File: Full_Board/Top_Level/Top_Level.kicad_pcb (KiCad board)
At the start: 2 copper layers, 174 x 97.8 mm, 223 parts, among them IC1 DRV8824QPWPRQ1, IC2 DRV8824QPWPRQ1, IC3 DRV8824QPWPRQ1, IC5 CD74HC4051PWT, IC6 CD74HC4051PWT, J1 OQ0212500000G, J1-J3 Conn_01x10, J10 KLDHCX-8-0202-A, J11 OQ0212500000G, J12 OQ0432500000G, J13 OQ0432500000G, J14 OQ0432500000G, J16 OQ0432500000G, J17 OQ0432500000G, J18 OQ0432500000G, J19 OQ0432500000G, J2 OQ0212500000G, J20 OQ0212500000G, J21 OQ0212500000G, J22 OQ0212500000G, J23 OQ0212500000G, J4-J2 Conn_01x10, J5-J7 Conn_01x10, J7 OQ0212500000G, J8 OQ0212500000G, J8-J6 Conn_01x10, J9 OQ0212500000G, U1 UCLAMP3301H.TCT, U10 LM2576SX-3.3-NOPB, U11 UCLAMP3301H.TCT, U12 UCLAMP3301H.TCT, U13 UCLAMP3301H.TCT, U14 UCLAMP3301H.TCT, U15 UCLAMP3301H.TCT, U16 UCLAMP3301H.TCT, U17 UCLAMP3301H.TCT, U18 UCLAMP3301H.TCT, U2 UCLAMP3301H.TCT, U3 UCLAMP3301H.TCT, U4 UCLAMP3301H.TCT, U5 UCLAMP3301H.TCT, U6 UCLAMP3301H.TCT, U7 JS102011SCQN, U8 UCLAMP3301H.TCT, U9 UCLAMP3301H.TCT

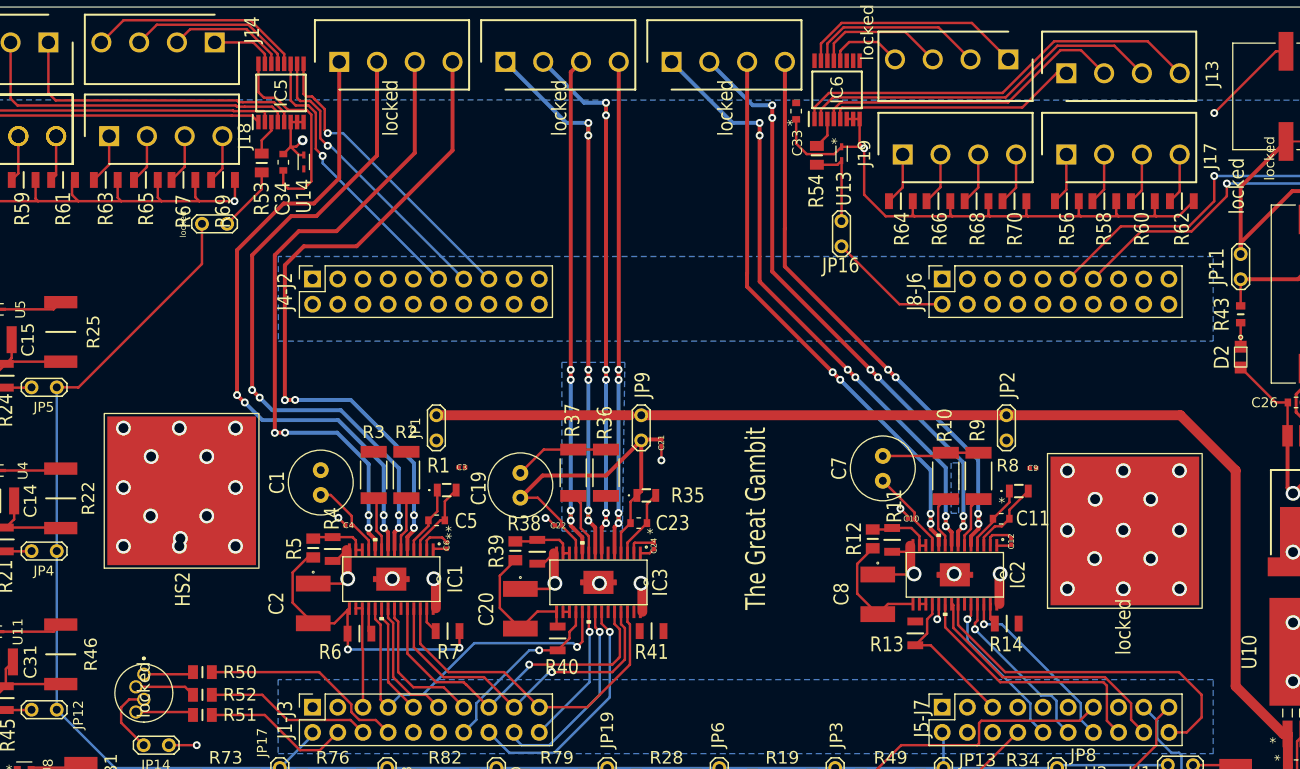
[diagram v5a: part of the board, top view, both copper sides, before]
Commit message: Only the truly awful traces left
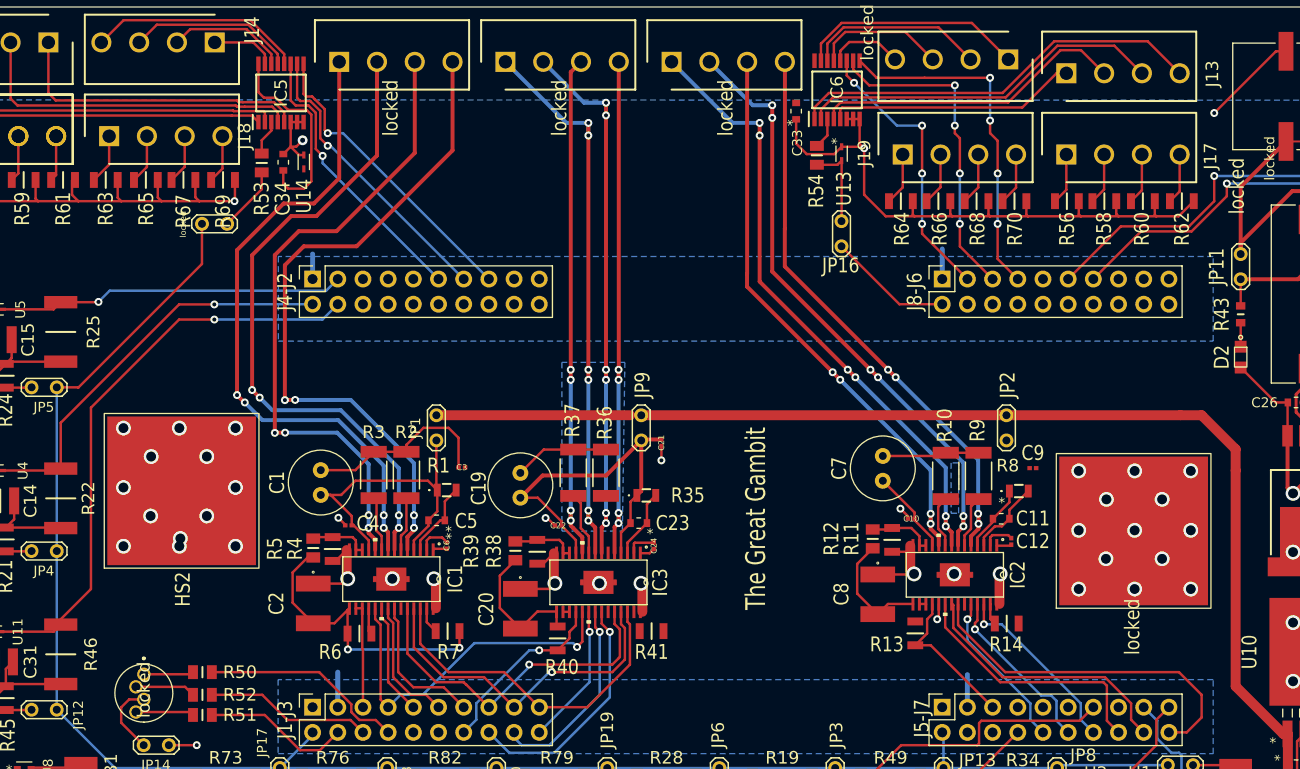
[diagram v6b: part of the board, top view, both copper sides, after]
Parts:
- moved locked 0.89 mm to (178.8, 91.4)
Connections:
- HS2 pad 1: (no net) -> GND
- J4-J2 pad 6: Y_HOME -> Y_FAULT
- J4-J2 pad 8: Y_FAULT -> Y_HOME
- locked pad 1: (no net) -> GND
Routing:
- net START_OUT: track 6.33 -> 58.7 mm, vias 0 -> 1
- net MUX_S2: track 0.00 -> 35.3 mm, vias 0 -> 4
- net RESET_OUT: track 5.95 -> 40.9 mm, vias 0 -> 1
- net MUX_S1: track 0.00 -> 32.9 mm, vias 0 -> 4
- net GND: track 428.4 -> 460.3 mm
- net HOME_OUT: track 6.17 -> 35.1 mm, vias 0 -> 1
- net MUX_S0: track 0.00 -> 28.5 mm, vias 0 -> 4
- net Net-(C1-Pad1): track 15.3 -> 33.1 mm
- net +24V: track 206.4 -> 207.7 mm

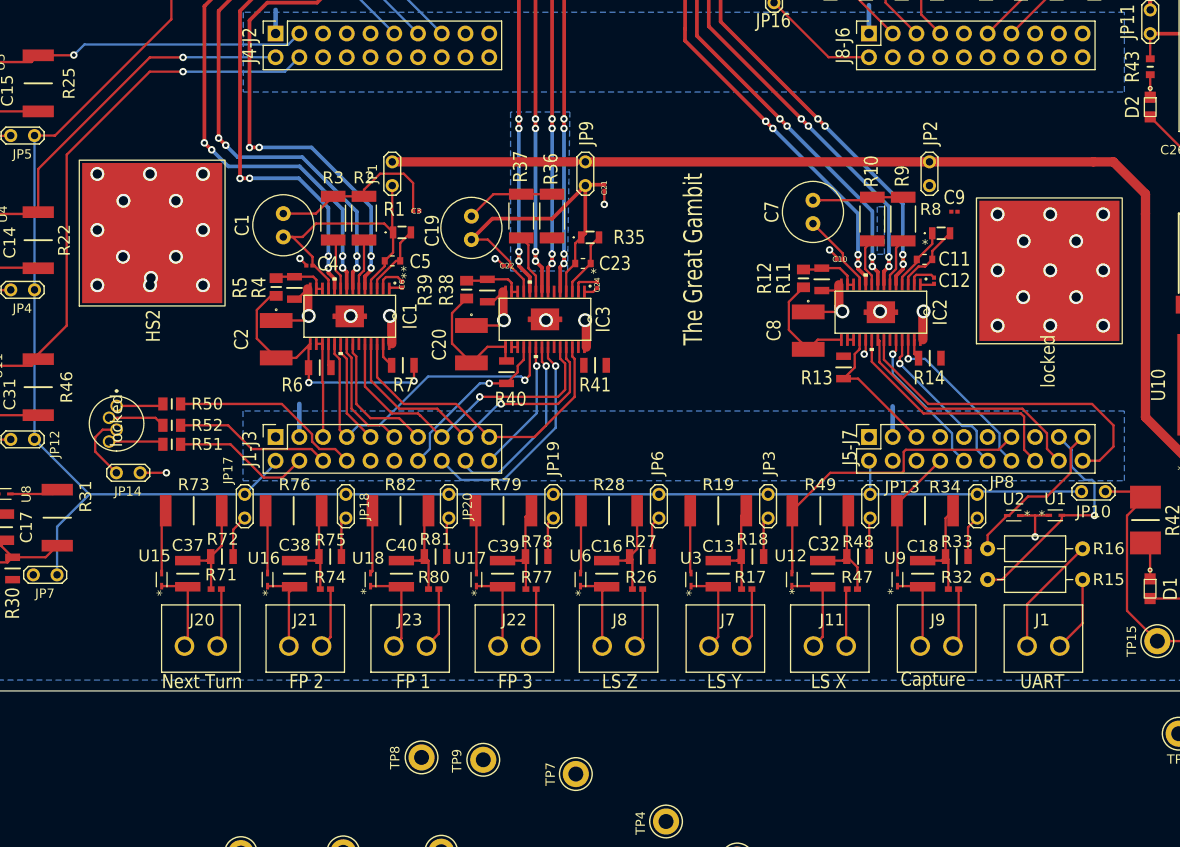
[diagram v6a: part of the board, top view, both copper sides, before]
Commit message: KiCad keeps crashing and getting rid of silkscreen
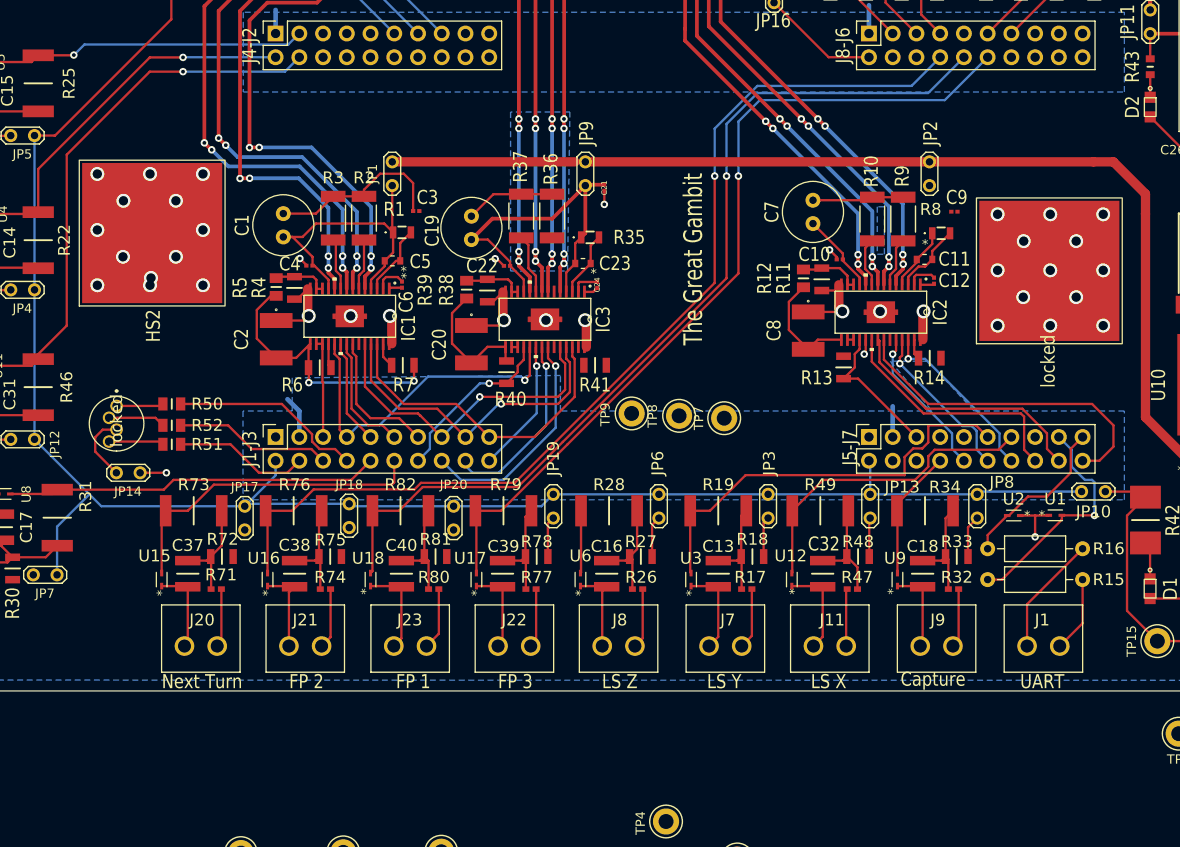
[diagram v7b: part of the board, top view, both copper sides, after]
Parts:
- moved TP8 45.8 mm to (139.2, 106.9)
- moved TP7 41.3 mm to (144.0, 107.2)
- moved TP9 40.3 mm to (134.1, 106.7)
- moved JP20 1.37 mm to (115.1, 116.6)
- moved JP17 1.27 mm to (92.7, 116.6)
- moved JP18 1.08 mm to (103.9, 116.4)
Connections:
- HS2 pad 1: GND -> (no net)
- J8-J6 pad 10: FP_2_OUT -> FP_1_OUT
- J8-J6 pad 8: FP_1_OUT -> FP_2_OUT
- locked pad 1: GND -> (no net)
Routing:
- net FP_2_OUT: track 6.75 -> 108.7 mm, vias 0 -> 1
- net FP_1_OUT: track 6.75 -> 99.8 mm, vias 0 -> 1
- net FP_3_OUT: track 6.71 -> 91.2 mm, vias 0 -> 1
- net LS_Y_OUT: track 6.71 -> 45.0 mm
- net COLOR_OUT: track 5.21 -> 40.0 mm
- net NEXT_TURN_OUT: track 6.85 -> 34.9 mm
- net Net-(JP17-Pad2): track 4.63 -> 0.00 mm
- net Net-(JP18-Pad2): track 4.32 -> 0.00 mm
- net Net-(JP20-Pad2): track 4.21 -> 0.00 mm
- net +3.3V: track 210.2 -> 212.7 mm
- net GND: track 460.3 -> 461.3 mm
- net LS_X_OUT: track 34.6 -> 34.1 mm

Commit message: KiCad hates silkscreen
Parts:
- moved TP14 43.8 mm to (225.8, 60.7)
- moved R14 3.50 mm to (167.9, 98.1), turned to -90 degrees
- moved locked 1.02 mm to (179.8, 91.4)
- moved C9 0.36 mm to (168.4, 84.8), turned to 0 degrees
- renumbered D4 to locked, D3 to locked
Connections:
- J5-J7 pad 10: Z_MS0 -> /MSP432E401Y/PD_4
- J5-J7 pad 12: Z_MS1 -> /MSP432E401Y/PD_5
- J5-J7 pad 14: Z_MS2 -> /MSP432E401Y/PQ_0
- J8-J6 pad 14: /MSP432E401Y/PH_0 -> Z_MS2
- J8-J6 pad 16: /MSP432E401Y/PH_1 -> Z_MS1
- J8-J6 pad 18: /MSP432E401Y/PK_6 -> Z_MS0
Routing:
- net XYZ_RESET: track 12.0 -> 86.5 mm, vias 0 -> 3
- net XYZ_DECAY: track 37.7 -> 95.5 mm, vias 2 -> 3
- net LS_Z_OUT: track 6.69 -> 51.0 mm, vias 0 -> 1
- net Z_MS0: track 16.2 -> 48.8 mm
- net Z_MS1: track 17.5 -> 45.8 mm
- net Z_MS2: track 18.5 -> 44.2 mm
- net Net-(C8-Pad2): track 12.1 -> 27.8 mm, vias 0 -> 2
- net Net-(C2-Pad2): track 30.2 -> 15.6 mm, vias 2 -> 0
- net Z_HOME: track 2.17 -> 13.8 mm, vias 0 -> 1
- net GND: track 461.3 -> 471.3 mm
- net Net-(C30-Pad1): track 38.5 -> 47.6 mm
- net Net-(C10-Pad2): track 15.5 -> 22.2 mm
- net X_HOME: track 0.00 -> 2.19 mm
